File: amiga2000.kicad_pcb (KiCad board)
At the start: 2 copper layers, 416.3 x 345.8 mm, 558 parts, among them CN200 DB9P RIGHT(1), CN201 DB9P LEFT(0), CN202 DB23M, CN203 INTERNAL VIDEO SLOT TOP, CN204 RIGHT AUDIO, CN205 LEFT AUDIO, CN206 COMPOSITE, CN207 INTERNAL VIDEO SLOT BOT, CN300 KEYBOARD, CN301 DB25F, CN302 DB23F, CN303 Conn_02x17_Odd_Even, CN304 Conn_02x13_Odd_Even, CN305 DB25M, CN306 Conn_01x03_Male, CN400 POWER_CONN, CN600 CO-PROCESSOR_SLOT, CN601 zorro_socket, CN602 zorro_socket, CN603 zorro_socket, CN604 zorro_socket, CN605 zorro_socket, CN606 Conn_01x04_Male, CN700 IBM_8_BIT_EXPANSION_BUS, CN701 IBM_8_BIT_EXPANSION_BUS, CN702 IBM_8_BIT_EXPANSION_BUS, CN703 IBM_8_BIT_EXPANSION_BUS, CN704 IBM_16_BIT_EXTENDED_BUS, CN705 IBM_16_BIT_EXTENDED_BUS, CN706 IBM_16_BIT_EXTENDED_BUS, CN707 IBM_16_BIT_EXTENDED_BUS, J1 Conn_01x03_Male, J101 Conn_01x03_Male, J102 Jumper_2_Open, J2 Conn_01x03_Male, J200 Conn_01x03_Male, J3 ACCEL, J300 Conn_01x03_Male, J301 DF1:, J500 Jumper_2_Bridged, J900 Jumper_2_Bridged, Q200 MPF102, Q201 MPF102, Q202 2N3906, Q300 2SC945, Q301 2N3904, Q302 2N3906, U1 PST518B, U100 MC68000, U101 AGNUS8372, U102 GARY5719, U103 74F245, U104 74LS373, U105 74F245, U106 74LS373, U107 74LS74A, U108 74LS74A, U200 PAULA, U201 DENISE8373, U202 74LS157, U203 74LS38, U204 LF347, U205 74LS244, U206 74LS244, U300 CIA8520, U301 8520, U302 74LS32, U303 74F08, U304 1488, U305 1489, U500 62402, U501 XX4256-15, U502 XX4256-15, U503 XX4256-15, U504 XX4256-15, U505 XX4256-15, U506 XX4256-15, U507 XX4256-15, U508 XX4256-15, U540 74F244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

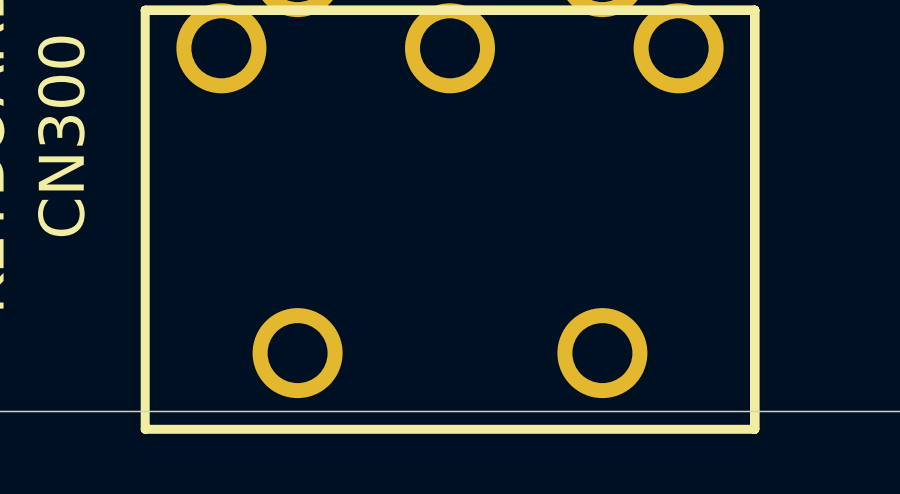
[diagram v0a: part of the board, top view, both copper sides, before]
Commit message: Din keyboard update
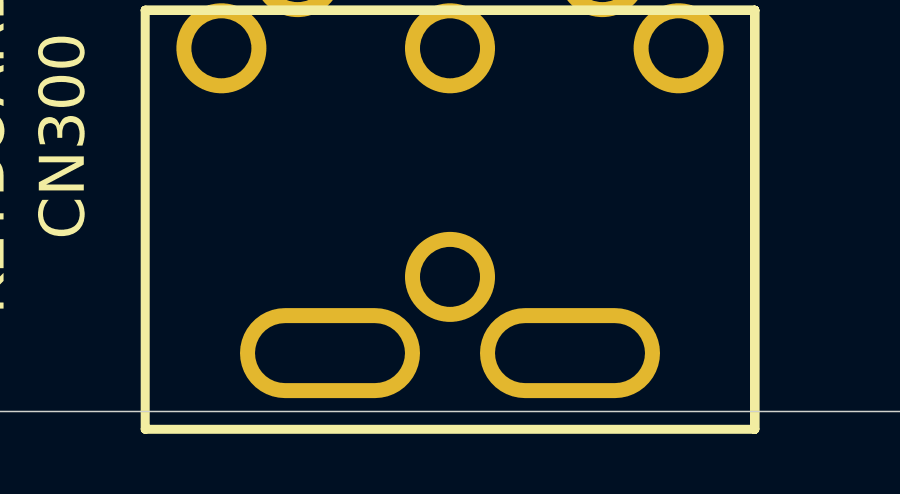
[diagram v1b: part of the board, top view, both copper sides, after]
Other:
- board text removed: "FIXME: 3 pads on front + the actual ones (compat with midi connector)"
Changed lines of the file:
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@@
   (general
     (thickness 1.6)
-    (drawings 225)
+    (drawings 224)
     (tracks 0)
     (zones 0)
@@
     (add_net -AV)
   )
+  (module d_amiga:DIN_5_KBD locked (layer F.Cu)
+    (at 312.5478 362.8934)
+    (descr "DIN 5 Amiga keyboard connector; Fits original and midi type connector")
+    (fp_text reference CN300 (at -12.9 2.925 90) (layer F.SilkS)
+      (effects (font (size 1.5 1.5) (thickness 0.15)))
+    )
+    (fp_text value KEYBOARD (at -15.575 3.2 90) (layer F.SilkS)
+      (effects (font (size 1.5 1.5) (thickness 0.15)))
+    )
+    (fp_line (start -10.16 -1.27) (end 10.16 -1.27) (layer F.SilkS) (width 0.3))
+    (fp_line (start -10.16 -1.27) (end -10.16 12.7) (layer F.SilkS) (width 0.3))
+    (fp_line (start 10.16 -1.27) (end -10.16 -1.27) (layer F.SilkS) (width 0.3))
+    (fp_line (start 10.16 12.7) (end 10.16 -1.27) (layer F.SilkS) (width 0.3))
+    (fp_line (start 10.16 -1.27) (end 10.16 12.7) (layer F.SilkS) (width 0.3))
+    (fp_line (start -10.16 12.7) (end 10.16 12.7) (layer F.SilkS) (width 0.3))
+    (pad "" thru_hole oval (at 4 10.16) (size 6 3) (drill oval 5 2) (layers *.Cu *.Mask))
+    (pad "" thru_hole oval (at -4 10.16) (size 6 3) (drill oval 5 2) (layers *.Cu *.Mask))
+    (pad "" thru_hole circle (at 0 7.62) (size 3 3) (drill 2) (layers *.Cu *.Mask))
+    (pad 1 thru_hole circle (at -7.62 0) (size 3 3) (drill 2) (layers *.Cu *.Mask)
+      (net 320 "Net-(CN300-Pad1)"))
+    (pad 4 thru_hole circle (at -5.08 -2.54) (size 3 3) (drill 2) (layers *.Cu *.Mask)
+      (net 35 "Net-(C259-Pad1)"))
+    (pad 2 thru_hole circle (at 0 0) (size 3 3) (drill 2) (layers *.Cu *.Mask)
+      (net 37 /parallel/_KBDATA))
+    (pad 5 thru_hole circle (at 5.08 -2.54) (size 3 3) (drill 2) (layers *.Cu *.Mask)
+      (net 1 GND))
+    (pad 3 thru_hole circle (at 7.62 0) (size 3 3) (drill 2) (layers *.Cu *.Mask)
+      (net 36 _KBCLK))
+  )
   (module Capacitor_THT:C_Rect_L11.5mm_W2.0mm_P10.00mm_MKT locked (layer F.Cu)
     (at 124.7628 141.2484 180)
@@
       (net 229 "/pc slots/A0"))
   )
-  (module d_amiga:DIN_5_KBD locked (layer F.Cu)
-    (at 312.5478 362.8934)
-    (fp_text reference CN300 (at -12.9 2.925 90) (layer F.SilkS)
-      (effects (font (size 1.5 1.5) (thickness 0.15)))
-    )
-    (fp_text value KEYBOARD (at -15.575 3.2 90) (layer F.SilkS)
-      (effects (font (size 1.5 1.5) (thickness 0.15)))
-    )
-    (fp_line (start -10.16 12.7) (end 10.16 12.7) (layer F.SilkS) (width 0.3))
-    (fp_line (start 10.16 -1.27) (end 10.16 12.7) (layer F.SilkS) (width 0.3))
-    (fp_line (start 10.16 12.7) (end 10.16 -1.27) (layer F.SilkS) (width 0.3))
-    (fp_line (start 10.16 -1.27) (end -10.16 -1.27) (layer F.SilkS) (width 0.3))
-    (fp_line (start -10.16 -1.27) (end -10.16 12.7) (layer F.SilkS) (width 0.3))
-    (fp_line (start -10.16 -1.27) (end 10.16 -1.27) (layer F.SilkS) (width 0.3))
-    (pad 3 thru_hole circle (at 7.62 0) (size 3 3) (drill 2) (layers *.Cu *.Mask)
-      (net 36 _KBCLK))
-    (pad 5 thru_hole circle (at 5.08 -2.54) (size 3 3) (drill 2) (layers *.Cu *.Mask)
-      (net 1 GND))
-    (pad 2 thru_hole circle (at 0 0) (size 3 3) (drill 2) (layers *.Cu *.Mask)
-      (net 37 /parallel/_KBDATA))
-    (pad 4 thru_hole circle (at -5.08 -2.54) (size 3 3) (drill 2) (layers *.Cu *.Mask)
-      (net 35 "Net-(C259-Pad1)"))
-    (pad 1 thru_hole circle (at -7.62 0) (size 3 3) (drill 2) (layers *.Cu *.Mask)
-      (net 320 "Net-(CN300-Pad1)"))
-    (pad "" thru_hole circle (at -5.08 10.16) (size 3 3) (drill 2) (layers *.Cu *.Mask))
-    (pad "" thru_hole circle (at 5.08 10.16) (size 3 3) (drill 2) (layers *.Cu *.Mask))
-  )
   (module d_amiga:VIDEOSLOT locked (layer F.Cu)
     (at 444.6478 91.1184 270)
@@
     (effects (font (size 2 2) (thickness 0.3)))
   )
-  (gr_text "FIXME: 3 pads on front + \nthe actual ones (compat \nwith midi connector)" (at 312.5978 382.8434) (layer Cmts.User)
-    (effects (font (size 1.5 1.5) (thickness 0.3)))
-  )
   (gr_text OUT (at 275.9978 221.2434 270) (layer F.SilkS)

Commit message: warning
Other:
- board text added: "/!\ BEWARE /!\ all connectors footprints are probably wrong (M vs F footprints mismatch pinout)"
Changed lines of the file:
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@@
   (general
     (thickness 1.6)
-    (drawings 224)
+    (drawings 225)
     (tracks 0)
     (zones 0)
@@
     )
   )
+  (gr_text "/!\\ BEWARE /!\\\nall connectors footprints are probably wrong (M vs F footprints mismatch pinout)" (at 323.3608 6.6444) (layer Cmts.User)
+    (effects (font (size 5 5) (thickness 0.5)))
+  )
   (gr_text "J301:\nclosed: A2000 override drive ID of 2nd\n    drive even if none installed. 3.5’’ work\nopen: drive should provide ID, no 2nd \n    drive or special HD drive 150rpm" (at 272.0528 121.4524) (layer F.SilkS)

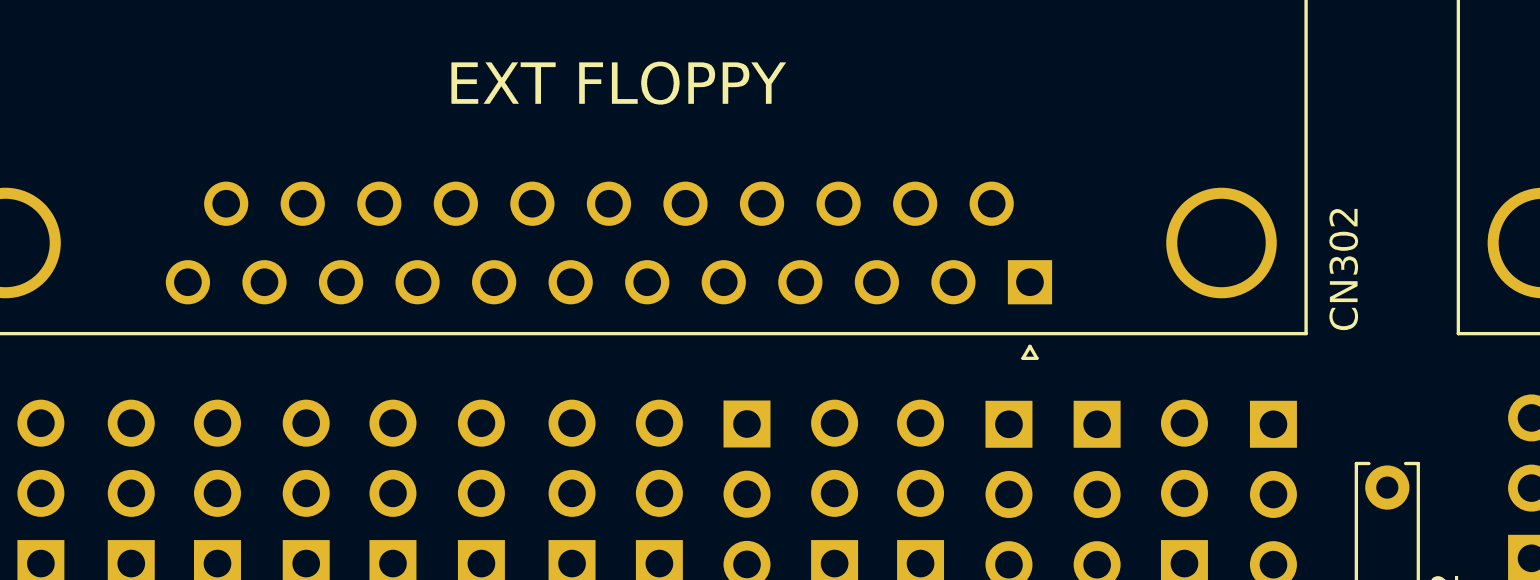
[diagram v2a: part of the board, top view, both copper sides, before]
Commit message: Now with F DB23, connectors are ok
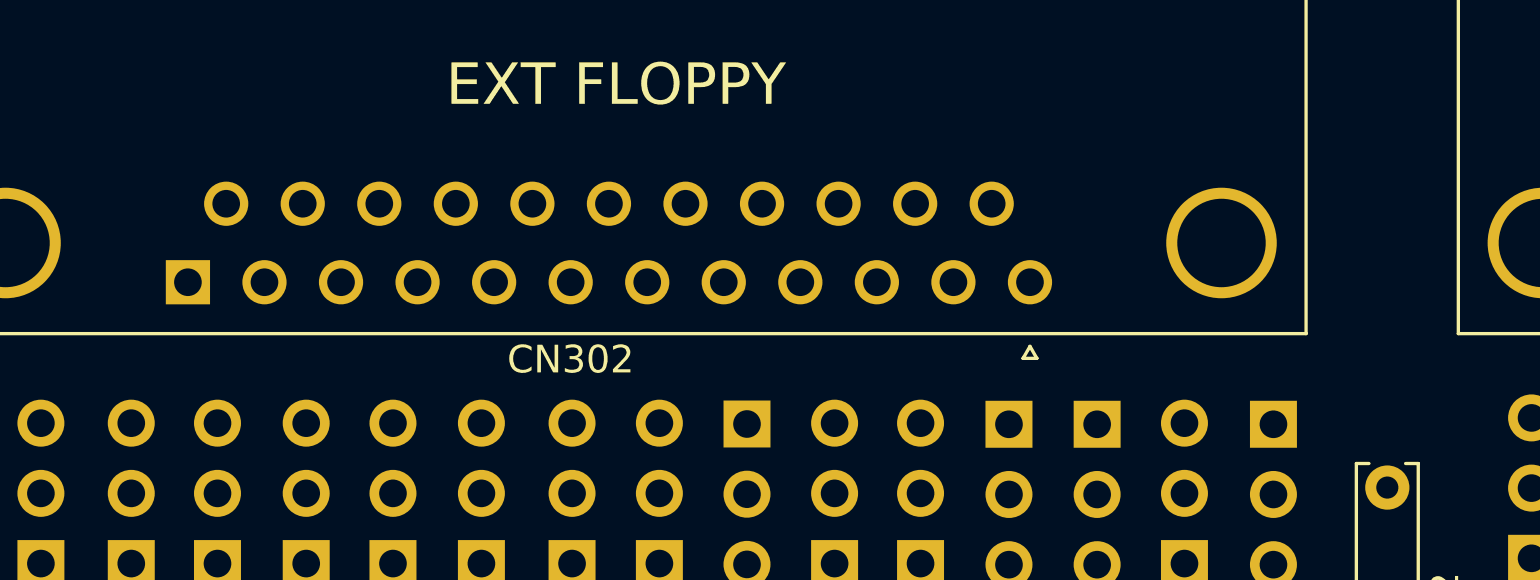
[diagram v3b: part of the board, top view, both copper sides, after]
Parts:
- CN302: footprint d_amiga:DSUB-23_Male_Horizontal_P2.77x2.84mm_EdgePinOffset7.70mm_Housed_MountingHolesOffset9.12mm -> d_amiga:DSUB-23_Female_Horizontal_P2.77x2.84mm_EdgePinOffset7.70mm_Housed_MountingHolesOffset9.12mm
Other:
- board text removed: "/!\ BEWARE /!\ all connectors footprints are probably wrong (M vs F footprints mismatch pinout)"

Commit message: Correct some components orientation
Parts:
- moved C915 12.3 mm to (431.2, 126.8), turned to 180 degrees
- moved C908 11.4 mm to (257.0, 197.1), turned to 0 degrees
- moved C206 10.5 mm to (388.4, 65.3), turned to 0 degrees
- moved C407 10.3 mm to (217.9, 171.9), turned to 90 degrees
- moved FB401 10.2 mm to (242.3, 83.7), turned to 90 degrees
- moved R231 10.2 mm to (267.5, 77.7), turned to 270 degrees
- moved R243 10.2 mm to (266.5, 47.0), turned to 270 degrees
- moved R206 10.2 mm to (289.5, 77.7), turned to 270 degrees
- moved R807 10.2 mm to (149.7, 123.4), turned to 270 degrees
- moved R110 10.2 mm to (304.3, 113.3), turned to 90 degrees
- moved R500 10.2 mm to (301.3, 113.3), turned to 90 degrees
- moved R307 10.2 mm to (149.3, 355.6), turned to 270 degrees
- moved R210 10.2 mm to (245.9, 87.9), turned to 90 degrees
- moved R308 10.2 mm to (152.4, 365.8), turned to 90 degrees
- moved R242 10.2 mm to (259.0, 87.9), turned to 90 degrees
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
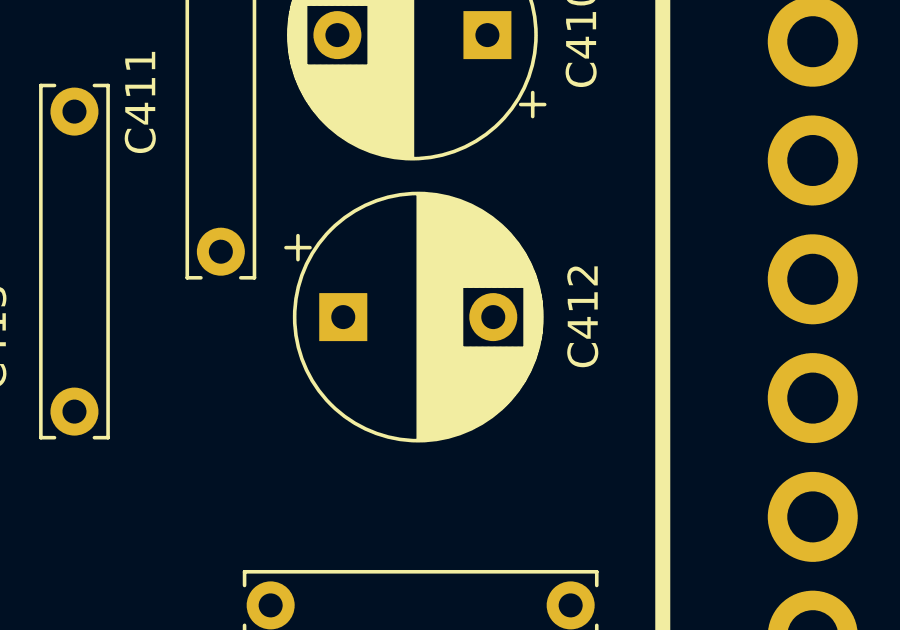
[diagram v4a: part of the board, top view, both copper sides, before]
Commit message: Fix capacitor error; regen files
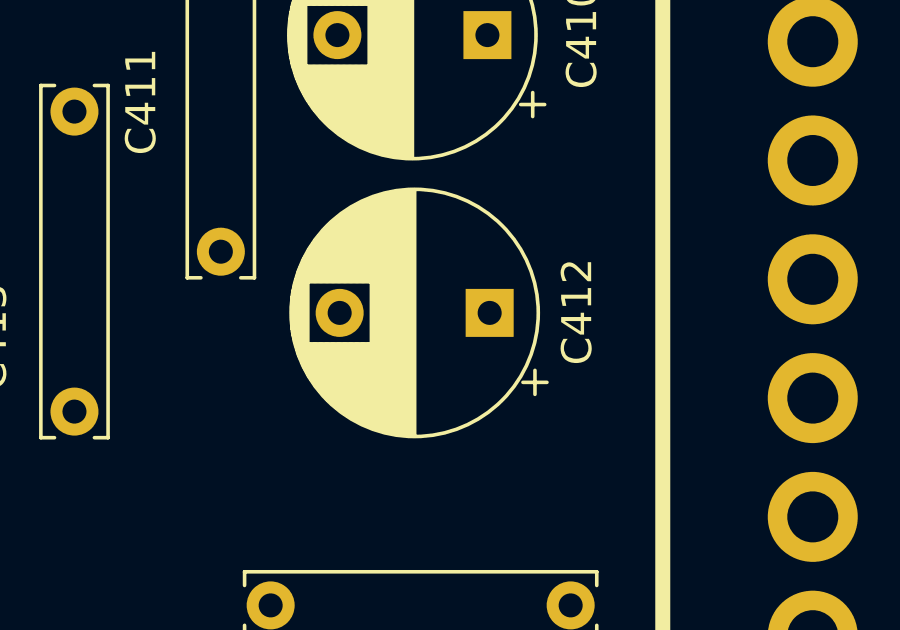
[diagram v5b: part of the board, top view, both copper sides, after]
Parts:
- moved C412 4.88 mm to (227.0, 187.4), turned to 180 degrees
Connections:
- C412 pad 1: GND -> -5V
- C412 pad 2: -5V -> GND
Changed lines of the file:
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@@
   )
   (module Capacitor_THT:CP_Radial_D8.0mm_P5.00mm locked (layer F.Cu)
-    (at 222.123 187.578)
+    (at 227.0028 187.4384 180)
     (descr "CP, Radial series, Radial, pin pitch=5.00mm, , diameter=8mm, Electrolytic Capacitor")
     (tags "CP Radial series Radial pin pitch 5.00mm  diameter 8mm Electrolytic Capacitor")
-    (fp_text reference C412 (at 8.02 -0.04 90) (layer F.SilkS)
+    (fp_text reference C412 (at -2.92 0.04 90) (layer F.SilkS)
       (effects (font (size 1 1) (thickness 0.15)))
     )
@@
     (fp_circle (center 2.5 0) (end 6.62 0) (layer F.SilkS) (width 0.12))
     (fp_circle (center 2.5 0) (end 6.5 0) (layer F.Fab) (width 0.1))
-    (pad 2 thru_hole circle (at 5 0) (size 1.6 1.6) (drill 0.8) (layers *.Cu *.Mask)
+    (pad 2 thru_hole circle (at 5 0 180) (size 1.6 1.6) (drill 0.8) (layers *.Cu *.Mask)
+      (net 1 GND))
+    (pad 1 thru_hole rect (at 0 0 180) (size 1.6 1.6) (drill 0.8) (layers *.Cu *.Mask)
       (net 17 -5V))
-    (pad 1 thru_hole rect (at 0 0) (size 1.6 1.6) (drill 0.8) (layers *.Cu *.Mask)
-      (net 1 GND))
     (model ${KISYS3DMOD}/Capacitor_THT.3dshapes/CP_Radial_D8.0mm_P5.00mm.wrl
       (at (xyz 0 0 0))

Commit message: Add DoNotPopulate field for components which shouldn't be fitted
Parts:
- moved J1 13.4 mm to (65.7, 335.7), turned to 270 degrees
- moved J2 9.15 mm to (78.9, 335.7), turned to 270 degrees

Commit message: Correct some datasheets
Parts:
- U107: value 74LS74A -> 74F04
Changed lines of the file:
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@@
       (effects (font (size 1 1) (thickness 0.15)))
     )
-    (fp_text value 74LS74A (at 3.81 17.57) (layer F.Fab)
+    (fp_text value 74F04 (at 3.81 17.57) (layer F.Fab)
       (effects (font (size 1 1) (thickness 0.15)))
     )
